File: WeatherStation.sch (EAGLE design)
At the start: 35 parts, among them J1 EDISON_CONNECTOR_FULLMOUNTING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, J2 EDISON_CONNECTOR_FULLHEADER, U1 MCP73831, U2 HTU21DSMD, U3 MPL3115A2LGA8, U4 PCA9306

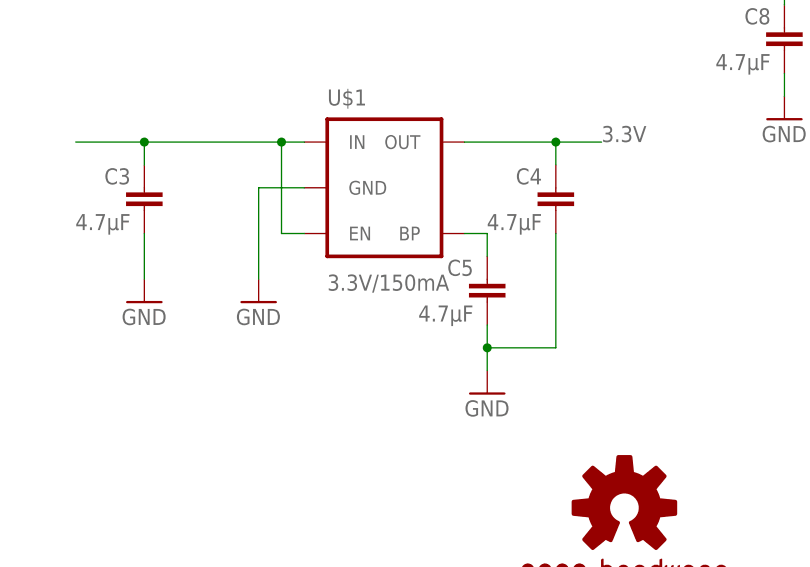
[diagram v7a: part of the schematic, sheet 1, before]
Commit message: rearranged silkscreens
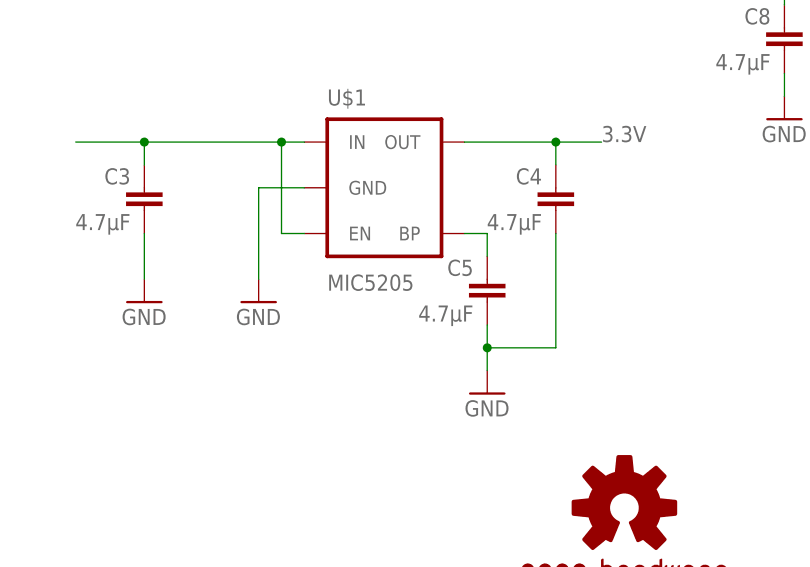
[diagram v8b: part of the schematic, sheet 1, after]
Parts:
- U$1: value 3.3V/150mA -> MIC5205
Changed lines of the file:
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@@
 <part name="U3" library="SparkFun-Sensors" deviceset="MPL3115A2" device="LGA8"/>
 <part name="U4" library="SparkFun-DigitalIC" deviceset="PCA9306" device="" value="PCA9306"/>
-<part name="U$1" library="SparkFun-PowerIC" deviceset="V_REG_MIC5205" device="3.3V" value="3.3V/150mA"/>
+<part name="U$1" library="SparkFun-PowerIC" deviceset="V_REG_MIC5205" device="3.3V" value="MIC5205"/>
 <part name="GND9" library="SparkFun-Aesthetics" deviceset="GND" device=""/>
 <part name="GND10" library="SparkFun-Aesthetics" deviceset="GND" device=""/>
